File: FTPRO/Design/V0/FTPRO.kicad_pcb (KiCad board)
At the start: 4 copper layers, 54 x 54 mm, 5 parts

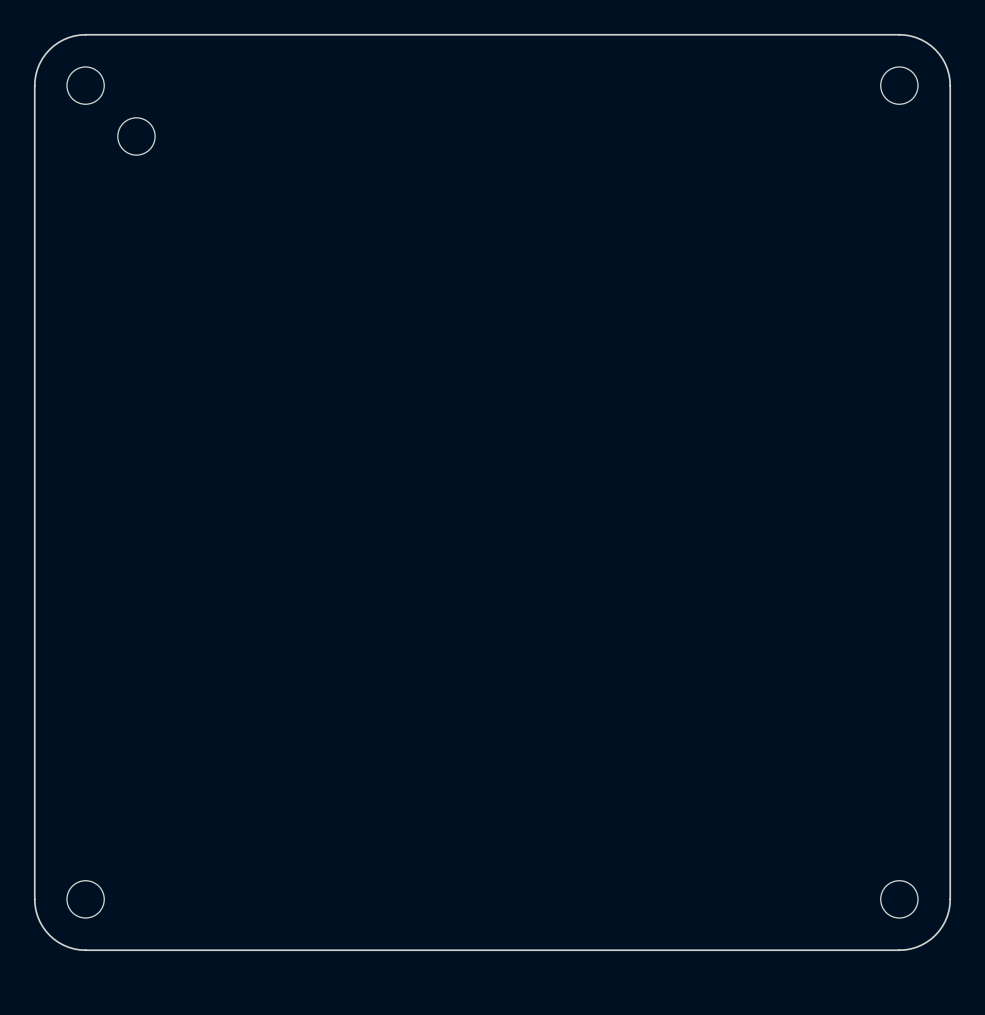
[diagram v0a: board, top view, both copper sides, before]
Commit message: PCB Outline
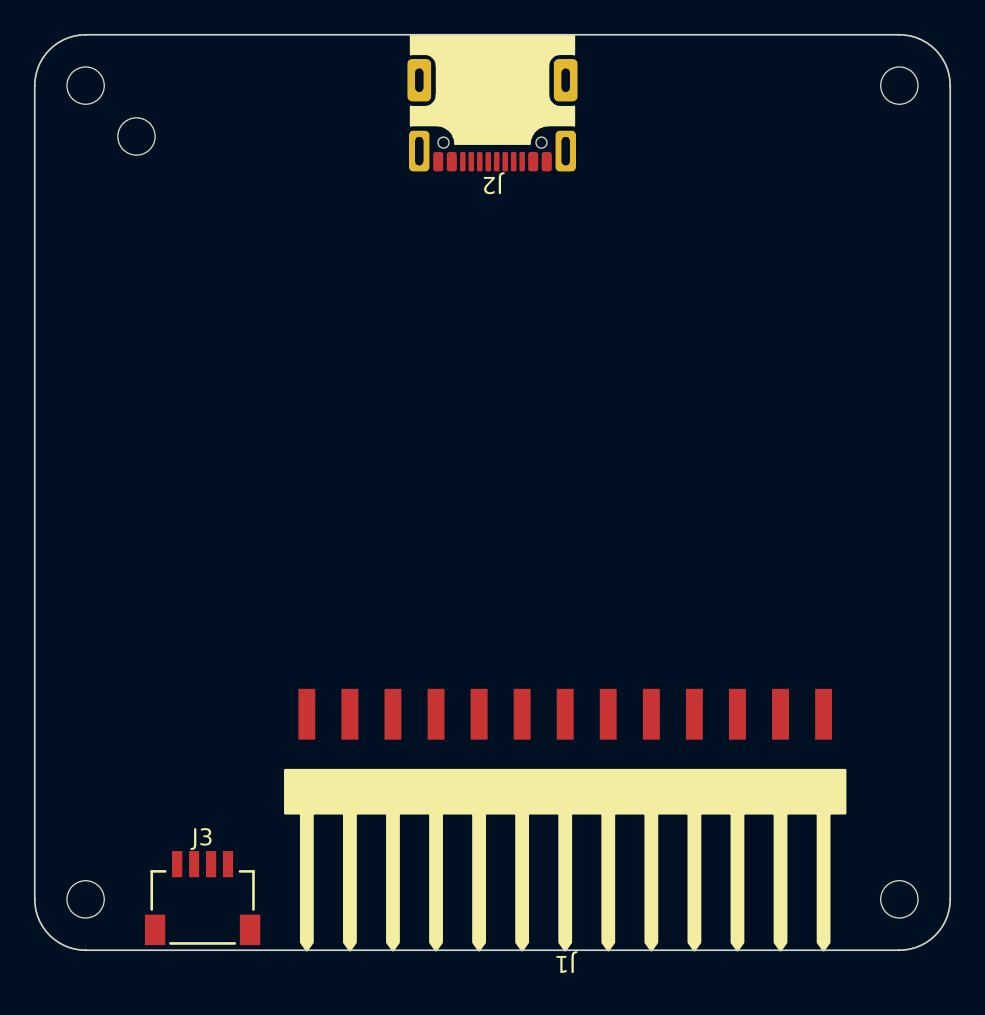
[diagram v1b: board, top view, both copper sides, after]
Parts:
- added J1: SIL13, Liem:HDM-1x13x2.54-SMD-RA, F.Cu at (128.3, 89.1)
- added J2: USB C, SAMPI:USB4105, F.Cu at (124.0, 53.7)
- added J3: QWIIC, SAMPI:HDM-1x4x1.0-RA, F.Cu at (106.9, 100.7)
